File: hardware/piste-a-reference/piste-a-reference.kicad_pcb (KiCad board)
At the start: 2 copper layers, 30 x 70 mm, 9 parts, among them Q1 BC33740BU C-B-E, U1 XIAO ESP32-C3

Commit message: fix: correct XIAO top-view pin orientation
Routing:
- net GND: track 45.7 -> 66.0 mm
- net +5V: track 38.1 -> 53.3 mm
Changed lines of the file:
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@@
     (pad "6" thru_hole circle (at 106.11 71.03) (size 1.8 1.8) (drill 1) (layers "*.Cu" "*.Mask"))
     (pad "7" thru_hole circle (at 106.11 73.57) (size 1.8 1.8) (drill 1) (layers "*.Cu" "*.Mask"))
-    (pad "14" thru_hole circle (at 121.35 58.33) (size 1.8 1.8) (drill 1) (layers "*.Cu" "*.Mask"))
-    (pad "13" thru_hole circle (at 121.35 60.87) (size 1.8 1.8) (drill 1) (layers "*.Cu" "*.Mask"))
-    (pad "12" thru_hole circle (at 121.35 63.41) (size 1.8 1.8) (drill 1) (layers "*.Cu" "*.Mask"))
-    (pad "11" thru_hole circle (at 121.35 65.95) (size 1.8 1.8) (drill 1) (layers "*.Cu" "*.Mask"))
-    (pad "10" thru_hole circle (at 121.35 68.49) (size 1.8 1.8) (drill 1) (layers "*.Cu" "*.Mask") (net 1 "+3V3"))
-    (pad "9" thru_hole circle (at 121.35 71.03) (size 1.8 1.8) (drill 1) (layers "*.Cu" "*.Mask") (net 4 "GND"))
-    (pad "8" thru_hole circle (at 121.35 73.57) (size 1.8 1.8) (drill 1) (layers "*.Cu" "*.Mask") (net 2 "+5V"))
+    (pad "8" thru_hole circle (at 121.35 58.33) (size 1.8 1.8) (drill 1) (layers "*.Cu" "*.Mask") (net 2 "+5V"))
+    (pad "9" thru_hole circle (at 121.35 60.87) (size 1.8 1.8) (drill 1) (layers "*.Cu" "*.Mask") (net 4 "GND"))
+    (pad "10" thru_hole circle (at 121.35 63.41) (size 1.8 1.8) (drill 1) (layers "*.Cu" "*.Mask") (net 1 "+3V3"))
+    (pad "14" thru_hole circle (at 121.35 65.95) (size 1.8 1.8) (drill 1) (layers "*.Cu" "*.Mask"))
+    (pad "13" thru_hole circle (at 121.35 68.49) (size 1.8 1.8) (drill 1) (layers "*.Cu" "*.Mask"))
+    (pad "12" thru_hole circle (at 121.35 71.03) (size 1.8 1.8) (drill 1) (layers "*.Cu" "*.Mask"))
+    (pad "11" thru_hole circle (at 121.35 73.57) (size 1.8 1.8) (drill 1) (layers "*.Cu" "*.Mask"))
   )
   (footprint "R1" (layer "F.Cu")
@@
   )
   (footprint "C1" (layer "F.Cu")
-    (property "Reference" "C1" (at 123.89 66.69) (layer "F.Fab") (effects (font (size 0.9 0.9) (thickness 0.15))))
-    (property "Value" "100 nF" (at 123.89 72.83) (layer "F.Fab") (effects (font (size 0.8 0.8) (thickness 0.15))) (hide yes))
-    (fp_rect (start 122.89 67.49) (end 124.89 72.03) (stroke (width 0.3) (type default)) (fill none) (layer "F.Fab"))
-    (pad "1" thru_hole rect (at 123.89 68.49) (size 1.8 1.8) (drill 1) (layers "*.Cu" "*.Mask") (net 1 "+3V3"))
-    (pad "2" thru_hole circle (at 123.89 71.03) (size 1.8 1.8) (drill 1) (layers "*.Cu" "*.Mask") (net 4 "GND"))
+    (property "Reference" "C1" (at 123.89 59.07) (layer "F.Fab") (effects (font (size 0.9 0.9) (thickness 0.15))))
+    (property "Value" "100 nF" (at 123.89 65.21) (layer "F.Fab") (effects (font (size 0.8 0.8) (thickness 0.15))) (hide yes))
+    (fp_rect (start 122.89 59.87) (end 124.89 64.41) (stroke (width 0.3) (type default)) (fill none) (layer "F.Fab"))
+    (pad "2" thru_hole circle (at 123.89 60.87) (size 1.8 1.8) (drill 1) (layers "*.Cu" "*.Mask") (net 4 "GND"))
+    (pad "1" thru_hole rect (at 123.89 63.41) (size 1.8 1.8) (drill 1) (layers "*.Cu" "*.Mask") (net 1 "+3V3"))
   )
   (footprint "C2" (layer "F.Cu")
@@
   (segment (start 113.73 81.19) (end 113.73 98.97) (width 0.55) (layer "B.Cu") (net 3))
   (segment (start 113.73 98.97) (end 113.73 104.05) (width 0.55) (layer "B.Cu") (net 3))
-  (segment (start 121.35 68.49) (end 123.89 68.49) (width 0.55) (layer "B.Cu") (net 1))
-  (segment (start 121.35 71.03) (end 123.89 71.03) (width 0.55) (layer "B.Cu") (net 4))
-  (segment (start 123.89 71.03) (end 123.89 104.05) (width 0.55) (layer "B.Cu") (net 4))
-  (segment (start 116.27 98.97) (end 123.89 98.97) (width 0.55) (layer "B.Cu") (net 4))
-  (segment (start 121.35 104.05) (end 123.89 104.05) (width 0.55) (layer "B.Cu") (net 4))
-  (segment (start 121.35 73.57) (end 126.43 73.57) (width 0.55) (layer "F.Cu") (net 2))
-  (segment (start 126.43 73.57) (end 126.43 106.59) (width 0.55) (layer "B.Cu") (net 2))
+  (segment (start 121.35 63.41) (end 123.89 63.41) (width 0.55) (layer "B.Cu") (net 1))
+  (segment (start 121.35 60.87) (end 123.89 60.87) (width 0.55) (layer "B.Cu") (net 4))
+  (segment (start 123.89 60.87) (end 118.81 60.87) (width 0.55) (layer "B.Cu") (net 4))
+  (segment (start 116.27 98.97) (end 118.81 98.97) (width 0.55) (layer "B.Cu") (net 4))
+  (segment (start 121.35 104.05) (end 118.81 104.05) (width 0.55) (layer "B.Cu") (net 4))
+  (segment (start 121.35 58.33) (end 126.43 58.33) (width 0.55) (layer "F.Cu") (net 2))
+  (segment (start 126.43 58.33) (end 126.43 106.59) (width 0.55) (layer "B.Cu") (net 2))
   (segment (start 116.27 106.59) (end 116.27 111.67) (width 0.55) (layer "B.Cu") (net 6))
   (segment (start 111.19 98.97) (end 108.65 98.97) (width 0.55) (layer "B.Cu") (net 7))
@@
   (segment (start 108.65 114.21) (end 118.81 114.21) (width 0.55) (layer "B.Cu") (net 7))
   (segment (start 118.81 114.21) (end 118.81 111.67) (width 0.55) (layer "B.Cu") (net 7))
-  (via (at 126.43 73.57) (size 1.8) (drill 1) (layers "F.Cu" "B.Cu") (net 2))
+  (segment (start 118.81 60.87) (end 118.81 98.97) (width 0.55) (layer "B.Cu") (net 4))
+  (segment (start 118.81 98.97) (end 123.89 98.97) (width 0.55) (layer "B.Cu") (net 4))
+  (segment (start 118.81 98.97) (end 118.81 104.05) (width 0.55) (layer "B.Cu") (net 4))
+  (segment (start 123.89 96.43) (end 123.89 98.97) (width 0.55) (layer "B.Cu") (net 4))
+  (segment (start 123.89 98.97) (end 123.89 101.51) (width 0.55) (layer "B.Cu") (net 4))
+  (via (at 126.43 58.33) (size 1.8) (drill 1) (layers "F.Cu" "B.Cu") (net 2))
 )

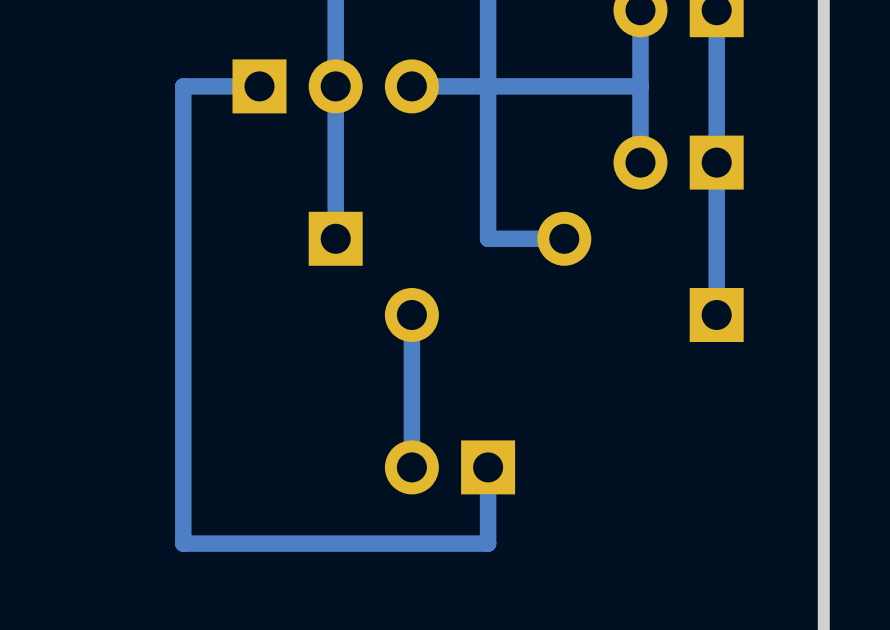
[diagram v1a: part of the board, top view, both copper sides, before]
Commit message: fix: match Piste A component lead spacing
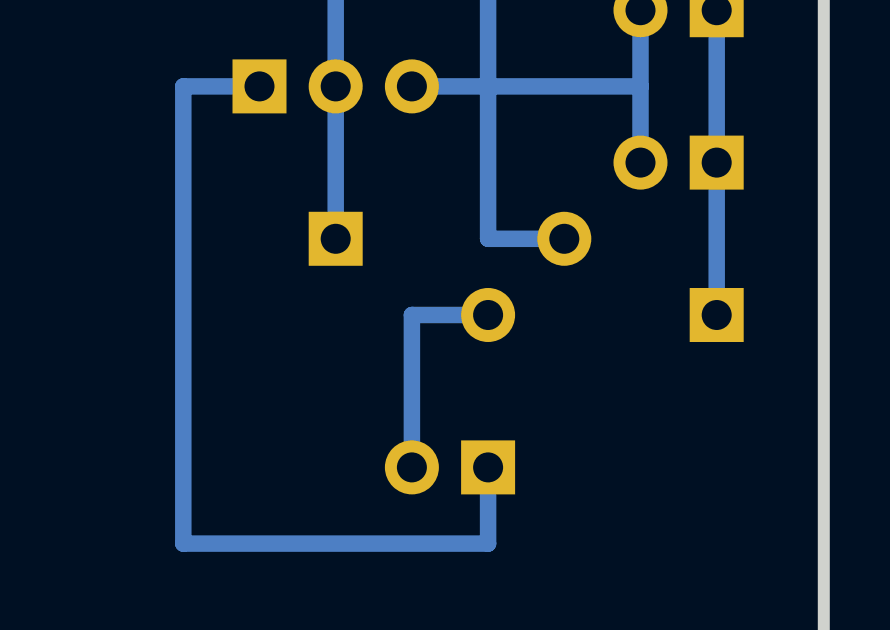
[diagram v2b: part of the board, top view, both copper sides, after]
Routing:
- net IR_ANODE: track 5.08 -> 7.62 mm
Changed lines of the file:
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@@
   )
   (footprint "R3" (layer "F.Cu")
-    (property "Reference" "R3" (at 121.35 104.79) (layer "F.Fab") (effects (font (size 0.9 0.9) (thickness 0.15))))
-    (property "Value" "47 ohm / 0.6 W" (at 121.35 108.39) (layer "F.Fab") (effects (font (size 0.8 0.8) (thickness 0.15))) (hide yes))
-    (fp_rect (start 115.27 105.59) (end 127.43 107.59) (stroke (width 0.3) (type default)) (fill none) (layer "F.Fab"))
+    (property "Reference" "R3" (at 122.62 104.79) (layer "F.Fab") (effects (font (size 0.9 0.9) (thickness 0.15))))
+    (property "Value" "47 ohm / 0.6 W" (at 122.62 108.39) (layer "F.Fab") (effects (font (size 0.8 0.8) (thickness 0.15))) (hide yes))
+    (fp_rect (start 117.81 105.59) (end 127.43 107.59) (stroke (width 0.3) (type default)) (fill none) (layer "F.Fab"))
     (pad "1" thru_hole rect (at 126.43 106.59) (size 1.8 1.8) (drill 1) (layers "*.Cu" "*.Mask") (net 2 "+5V"))
-    (pad "2" thru_hole circle (at 116.27 106.59) (size 1.8 1.8) (drill 1) (layers "*.Cu" "*.Mask") (net 6 "IR_ANODE"))
+    (pad "2" thru_hole circle (at 118.81 106.59) (size 1.8 1.8) (drill 1) (layers "*.Cu" "*.Mask") (net 6 "IR_ANODE"))
   )
   (footprint "D1" (layer "F.Cu")
@@
   (segment (start 123.89 96.43) (end 123.89 98.97) (width 0.55) (layer "B.Cu") (net 4))
   (segment (start 123.89 98.97) (end 123.89 101.51) (width 0.55) (layer "B.Cu") (net 4))
+  (segment (start 118.81 106.59) (end 116.27 106.59) (width 0.55) (layer "B.Cu") (net 6))
   (via (at 126.43 58.33) (size 1.8) (drill 1) (layers "F.Cu" "B.Cu") (net 2))
 )
